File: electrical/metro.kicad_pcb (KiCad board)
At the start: 2 copper layers, 28 x 14 mm, 44 parts, among them Q1 AO3401A, Q2 AO3400A, SW1 SW_Push, SW2 SW_Push, SW3 SW_Push, U1 ATTINY1616-MN, U2 MCP73831-2-OT, U3 XC6206PxxxMR, Y1 32.678

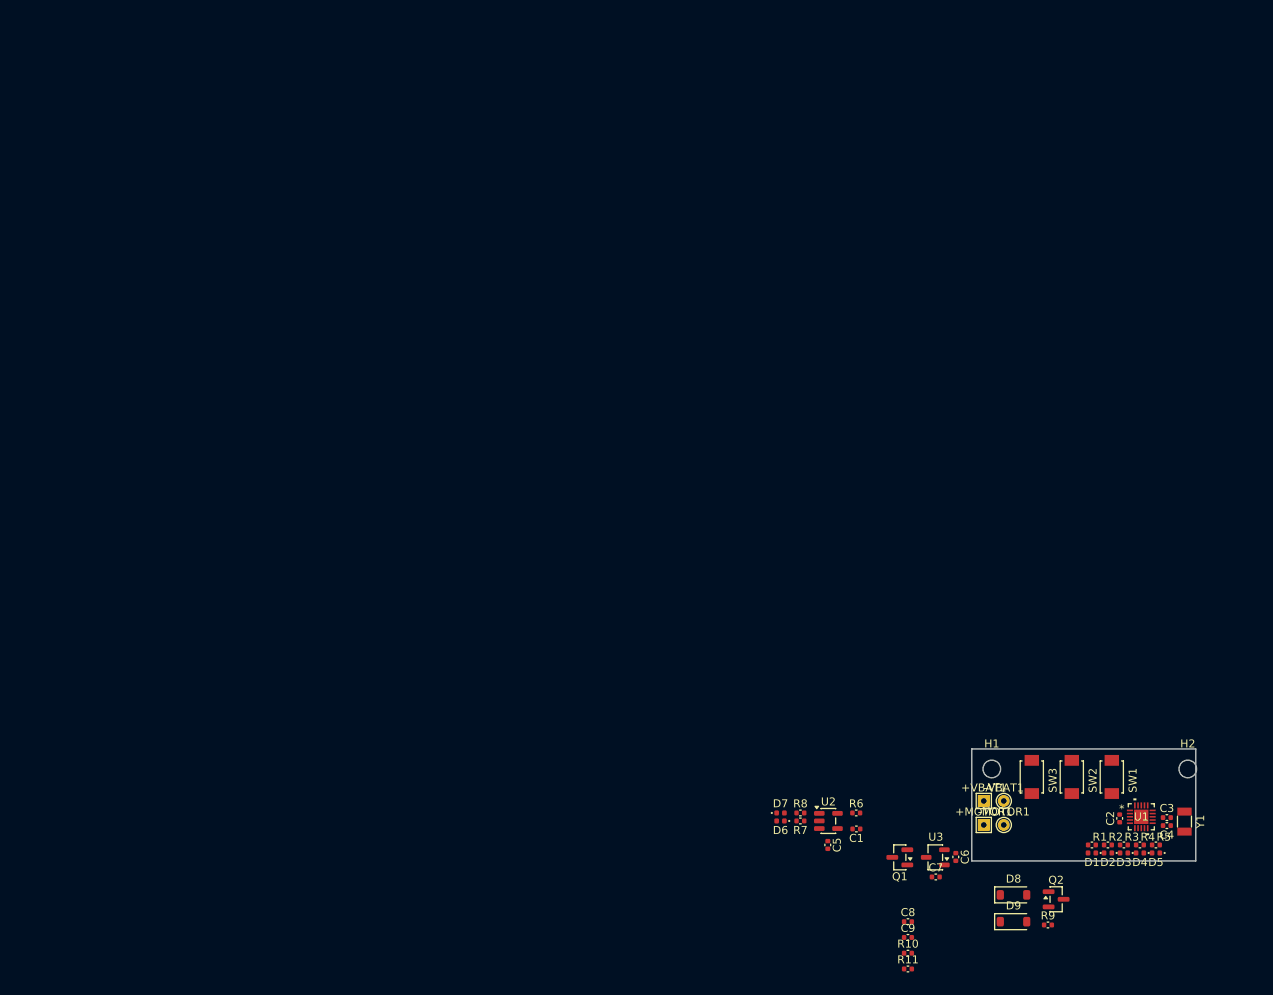
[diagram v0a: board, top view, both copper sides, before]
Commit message: Basic vibration with breakout board
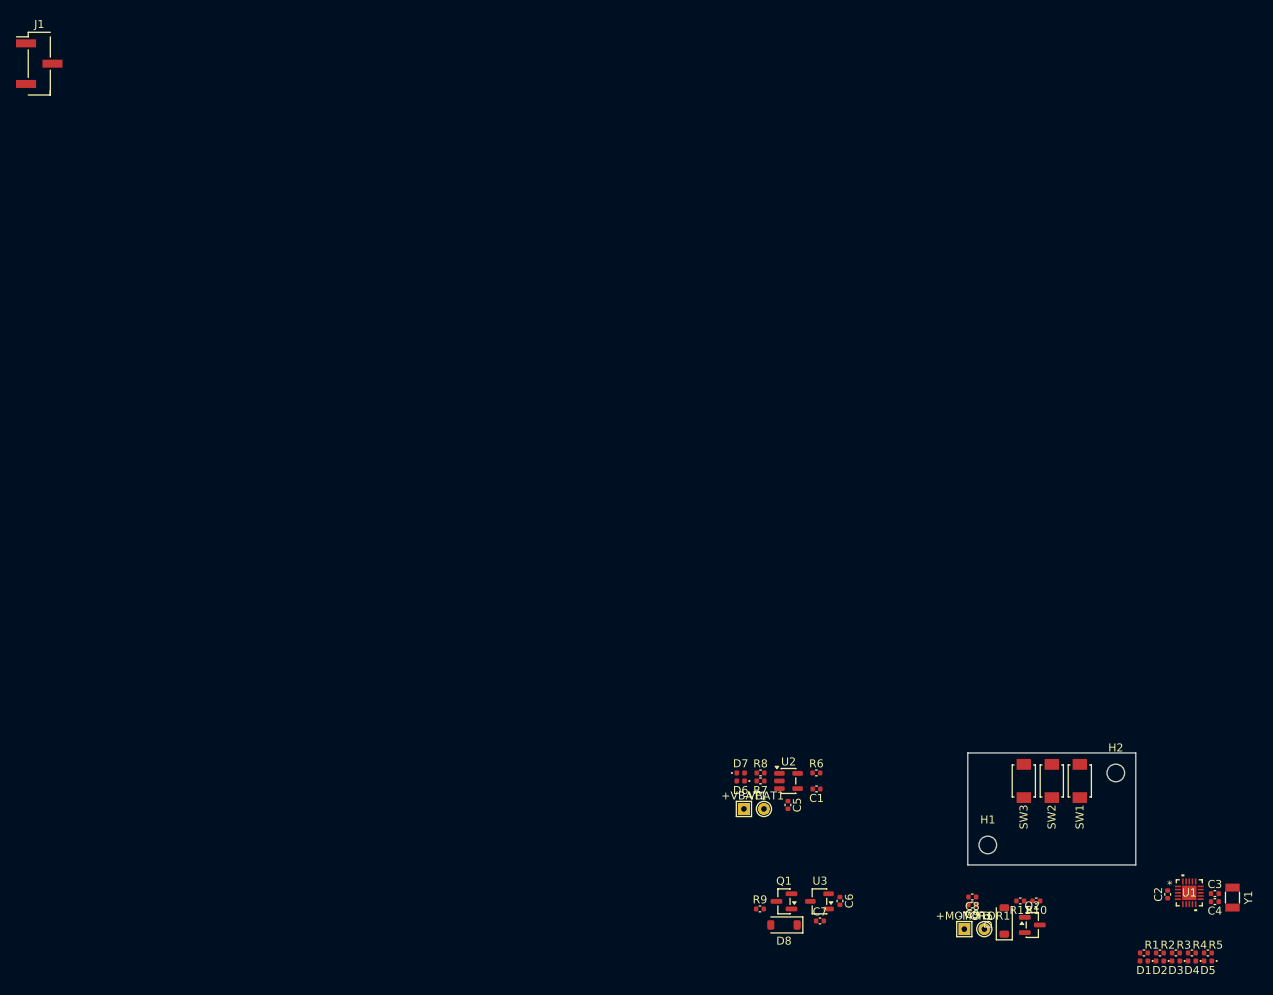
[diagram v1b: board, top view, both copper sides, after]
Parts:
- added J1: Conn_01x03_Pin, Connector_PinHeader_2.54mm:PinHeader_1x03_P2.54mm_Vertical_SMD_Pin1Left, F.Cu at (3.44, 4.33)
- moved R9 36.1 mm to (93.5, 110.0)
- moved +VBAT1 30.0 mm to (91.5, 97.5)
- moved -VBAT1 30.0 mm to (94.0, 97.5)
- moved D8 28.9 mm to (96.5, 112.0), turned to 180 degrees
- moved R10 17.3 mm to (128.1, 109.0), turned to 180 degrees
- moved R11 16.4 mm to (126.1, 109.0), turned to 180 degrees
- moved C6 15.5 mm to (103.5, 109.0)
- moved C7 15.5 mm to (101.0, 111.5)
- moved Q1 15.5 mm to (96.5, 109.0)
- moved U3 15.5 mm to (101.0, 109.0)
- moved D1 15.0 mm to (141.5, 116.5)
- moved D2 15.0 mm to (143.5, 116.5)
- moved D3 15.0 mm to (145.5, 116.5)
- moved D4 15.0 mm to (147.5, 116.5)
- moved D5 15.0 mm to (149.5, 116.5)
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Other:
- board size 28 x 14 mm -> 21 x 14 mm

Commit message: Circuit mostly complete with driver
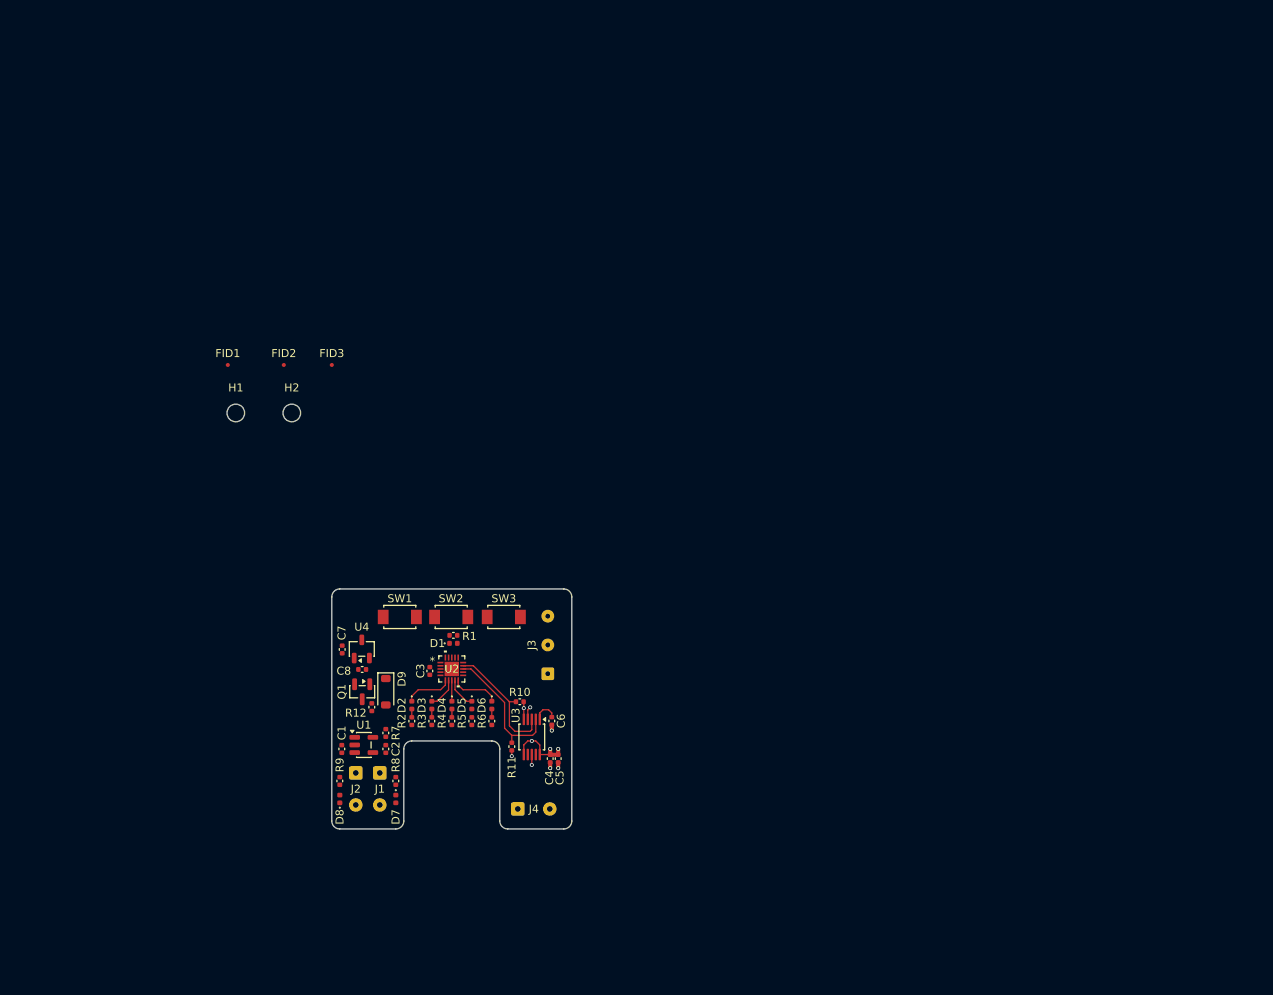
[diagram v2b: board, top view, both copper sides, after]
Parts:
- removed +MOTOR1, +VBAT1: ~, TestPoint:TestPoint_THTPad_1.5x1.5mm_Drill0.7mm
- removed -MOTOR1, -VBAT1: ~, TestPoint:TestPoint_THTPad_D1.5mm_Drill0.7mm
- removed the C3 at (150.4, 108.1)
- removed the C8 at (120.1, 108.5)
- removed C9: 10μF, Capacitor_SMD:C_0402_1005Metric
- removed the D9 at (124.1, 111.5)
- removed Q2: AO3400A, Package_TO_SOT_SMD:SOT-23
- removed Y1: 32.678, Crystal:Crystal_SMD_3215-2Pin_3.2x1.5mm
- added C5: 10μF, Capacitor_SMD:C_0402_1005Metric, F.Cu at (68.3, 91.2)
- added C6: 1μF, Capacitor_SMD:C_0402_1005Metric, F.Cu at (67.5, 86.5)
- added D1: Blue, LED_SMD:LED_0402_1005Metric, F.Cu at (55.2, 76.8)
- added FID1: Fiducial, Fiducial:Fiducial_0.5mm_Mask1mm, F.Cu at (27.0, 42.0)
- added FID2: Fiducial, Fiducial:Fiducial_0.5mm_Mask1mm, F.Cu at (34.0, 42.0)
- added FID3: Fiducial, Fiducial:Fiducial_0.5mm_Mask1mm, F.Cu at (40.0, 42.0)
- added J2: Conn_01x02, Connector_Wire:SolderWire-0.15sqmm_1x02_P4mm_D0.5mm_OD1.5mm, F.Cu at (43.0, 93.0)
- added J3: Conn_01x03, Connector_Wire:SolderWire-0.1sqmm_1x03_P3.6mm_D0.4mm_OD1mm, F.Cu at (67.0, 80.6)
- added J4: Conn_01x02, Connector_Wire:SolderWire-0.15sqmm_1x02_P4mm_D0.5mm_OD1.5mm, F.Cu at (63.2, 97.5)
- added R1: 2k2, Capacitor_SMD:C_0402_1005Metric, F.Cu at (55.2, 75.8)
- added U3: DRV2605LDGS, Package_SO:VSSOP-10_3x3mm_P0.5mm, F.Cu at (65.0, 88.5)
- C4: value 20pF -> 1μF
- J1: value Conn_01x03_Pin -> Conn_01x02; footprint Connector_PinHeader_2.54mm:PinHeader_1x03_P2.54mm_Vertical_SMD_Pin1Left -> Connector_Wire:SolderWire-0.15sqmm_1x02_P4mm_D0.5mm_OD1.5mm
- R10: value 100kR -> 4k7
- R11: value 100R -> 4k7
- R2: renamed from R1; value 680R -> 2k2
- R3: renamed from R2; value 680R -> 2k2
- R4: renamed from R3; value 680R -> 2k2
- R5: renamed from R4; value 680R -> 2k2
- R6: renamed from R5; value 680R -> 2k2
- R7: renamed from R6; value 10kR -> 33k
- R8: renamed from R7; value 680R -> 2k2
- R9: renamed from R8; value 680R -> 10k
- U1: renamed from U2; value MCP73831-2-OT -> MCP73831T-2ACI/OT
- U4: renamed from U3; value XC6206PxxxMR -> XC6206P332MR-G
- moved H2 112.4 mm to (35.0, 48.0)
- moved H1 108.4 mm to (28.0, 48.0)
- moved J1 98.4 mm to (46.0, 93.0), turned to -90 degrees
- moved D2 96.9 mm to (50.0, 84.5), turned to -90 degrees
- moved D3 96.5 mm to (52.5, 84.5), turned to -90 degrees
- moved C3 96.4 mm to (52.2, 80.2)
- moved U2 96.3 mm to (55.0, 80.0)
- moved R2 96.0 mm to (50.0, 86.5), turned to 90 degrees
- moved D4 96.0 mm to (55.0, 84.5), turned to -90 degrees
- moved D5 95.5 mm to (57.5, 84.5), turned to -90 degrees
- moved R3 95.5 mm to (52.5, 86.5), turned to 90 degrees
- moved D6 95.1 mm to (60.0, 84.5), turned to -90 degrees
- moved R4 95.0 mm to (55.0, 86.5), turned to 90 degrees
- moved R5 94.6 mm to (57.5, 86.5), turned to 90 degrees
- moved R6 94.1 mm to (60.0, 86.5), turned to 90 degrees
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- renumbered C5 to C1, C1 to C2, C2 to C3, C6 to C8, D1 to D2, D2 to D3, D3 to D4, D4 to D5, D5 to D6, D6 to D7, D7 to D8, D8 to D9, R9 to R12, SW3 to SW1, SW1 to SW3, U1 to U2
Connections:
- net +VBAT renamed +BATT
- net Net-(U2-STAT) renamed /LIPO STAT
- C2 pad 1: +5V -> +VBUS
- C4 pad 1: Net-(U1A-PB3/TOSC1) -> +3V3
- D7 pad 2: +5V -> +VBUS
- D9 pad 2: +5V -> +VBUS
- J1 pad 1: unconnected-(J1-Pin_1-Pad1) -> +VBUS
- J1 pad 2: unconnected-(J1-Pin_2-Pad2) -> GND
- Q1 pad 1: +5V -> +VBUS
- R10 pad 1: GND -> /SCL
- R10 pad 2: /MOTOR -> +3V3
- R11 pad 1: Net-(Q2-G) -> /SDA
- R11 pad 2: /MOTOR -> +3V3
- R12 pad 2: +5V -> +VBUS
- SW1 pad 1: GND -> /SW1
- SW1 pad 2: Net-(U1A-PC3) -> GND
- SW2 pad 1: GND -> /SW2
- SW2 pad 2: Net-(U1A-PC2) -> GND
- SW3 pad 1: GND -> /SW3
- SW3 pad 2: Net-(U1A-PC1) -> GND
- U1 pad 4: +5V -> +VBUS
- U2 pad 1: unconnected-(U1A-PA2-Pad1) -> /SW1
- U2 pad 11: Net-(U1A-PB3/TOSC1) -> unconnected-(U2A-PB3/TOSC1-Pad11)
- U2 pad 12: Net-(U1A-PB2/TOSC2) -> /SW2
- U2 pad 13: unconnected-(U1A-PB1-Pad13) -> /SDA
- U2 pad 14: unconnected-(U1A-PB0-Pad14) -> /SCL
- U2 pad 15: unconnected-(U1A-PC0-Pad15) -> /STATUS
- U2 pad 16: Net-(U1A-PC1) -> unconnected-(U2A-PC1-Pad16)
- U2 pad 17: Net-(U1A-PC2) -> /SW3
- U2 pad 18: Net-(U1A-PC3) -> unconnected-(U2A-PC3-Pad18)
- U2 pad 19: /UDPI -> /UPDI
- U2 pad 5: /LED1 -> unconnected-(U2A-PA4-Pad5)
- U2 pad 6: /MOTOR -> /LED1
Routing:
- net /SDA: track 0.00 -> 17.1 mm
- net /SCL: track 0.00 -> 15.7 mm
- net +3V3: track 0.00 -> 11.5 mm, vias 0 -> 5
- net /LED5: track 0.00 -> 5.99 mm
- net /LED1: track 0.00 -> 5.99 mm
- net GND: track 0.00 -> 5.08 mm, vias 0 -> 5
- net /LED2: track 0.00 -> 3.87 mm
- net /LED4: track 0.00 -> 3.87 mm
- net Net-(U3-REG): track 0.00 -> 3.15 mm
- net /LED3: track 0.00 -> 2.62 mm
- net Net-(D4-A): track 0.00 -> 1.04 mm
- net Net-(D6-A): track 0.00 -> 1.04 mm
- net Net-(D3-A): track 0.00 -> 1.04 mm
- net Net-(D2-A): track 0.00 -> 1.04 mm
- added copper zone on In2.Cu, net +3V3
- added copper zone on In1.Cu, net GND
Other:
- board size 21 x 14 mm -> 30 x 30 mm
- copper layers 2 -> 4

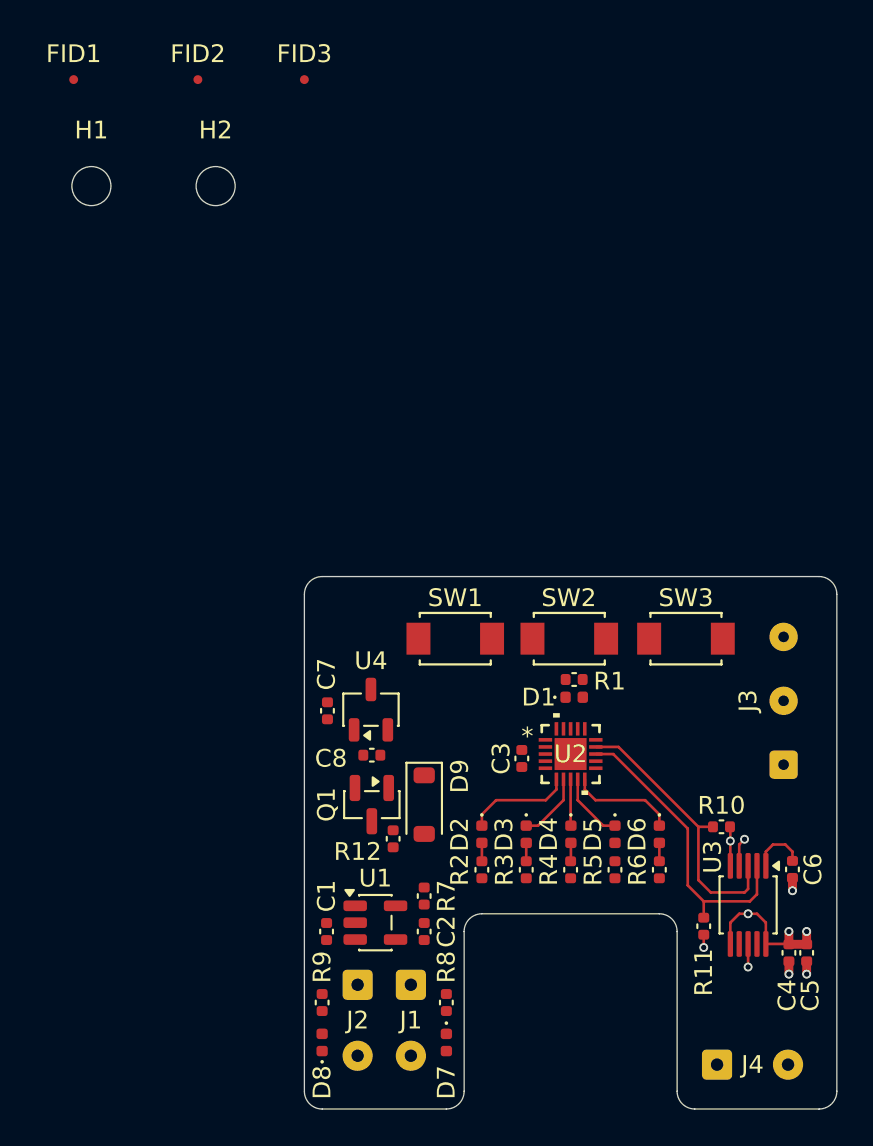
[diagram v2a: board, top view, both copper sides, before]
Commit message: new led setup
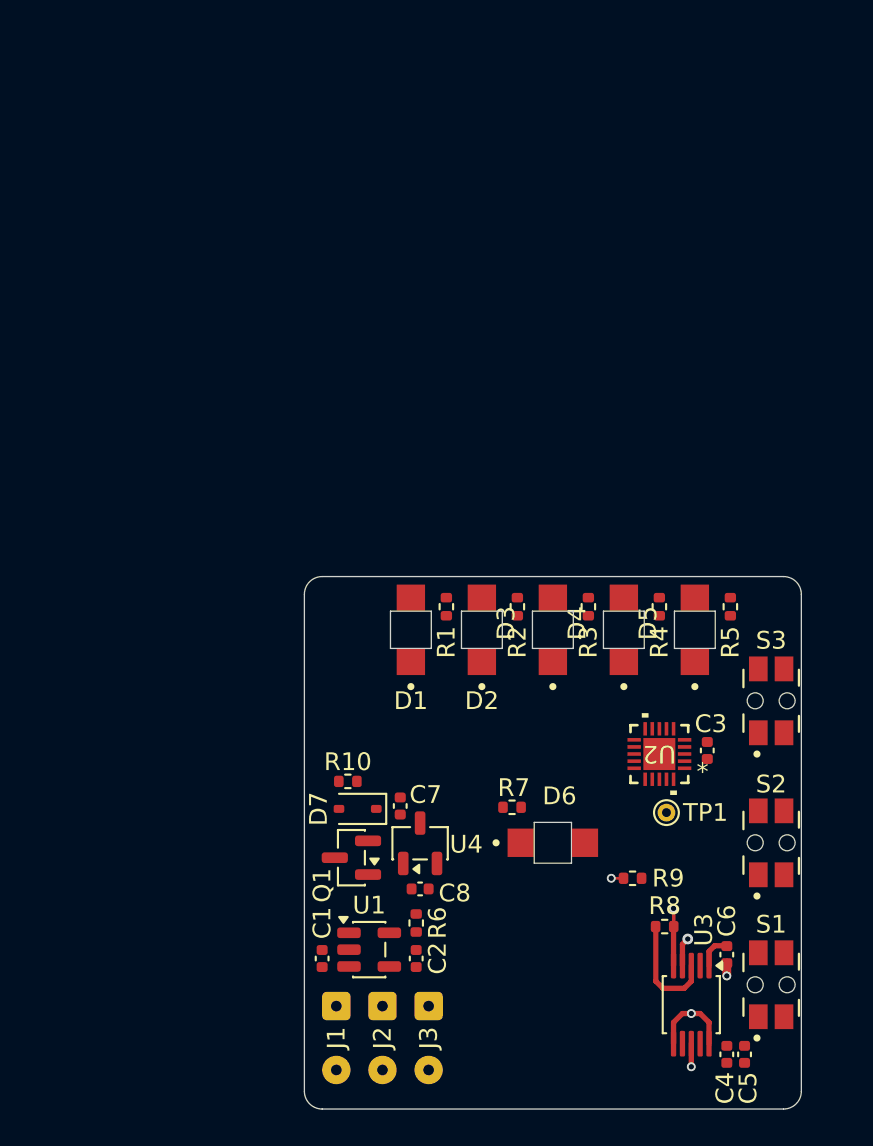
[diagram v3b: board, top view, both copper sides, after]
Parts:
- removed the D1 at (55.2, 76.8)
- removed D8: Green, LED_SMD:LED_0402_1005Metric
- removed FID1, FID2, FID3: Fiducial, Fiducial:Fiducial_0.5mm_Mask1mm
- removed H1, H2: M2, MountingHole:MountingHole_2.2mm_M2
- removed the J3 at (67.0, 80.6)
- removed the R1 at (55.2, 75.8)
- removed the R9 at (41.0, 94.0)
- removed SW1, SW2, SW3: SW_Push, TS-1088-AR02016:SW_TS-1088-AR02016
- added S1: EVQ-P7C01P, EVQ-P7C01P:SW_EVQ-P7C01P, F.Cu at (66.3, 93.0)
- added S2: EVQ-P7C01P, EVQ-P7C01P:SW_EVQ-P7C01P, F.Cu at (66.3, 85.0)
- added S3: EVQ-P7C01P, EVQ-P7C01P:SW_EVQ-P7C01P, F.Cu at (66.3, 77.0)
- added TP1: UPDI, TestPoint:TestPoint_THTPad_D1.0mm_Drill0.5mm, F.Cu at (60.4, 83.3)
- D1: renamed from D2; footprint LED_SMD:LED_0402_1005Metric -> LTST-C230KRKT:LED_LTST-C230KRKT
- D2: renamed from D3; footprint LED_SMD:LED_0402_1005Metric -> LTST-C230KRKT:LED_LTST-C230KRKT
- D3: renamed from D4; footprint LED_SMD:LED_0402_1005Metric -> LTST-C230KRKT:LED_LTST-C230KRKT
- D4: renamed from D5; footprint LED_SMD:LED_0402_1005Metric -> LTST-C230KRKT:LED_LTST-C230KRKT
- D5: renamed from D6; footprint LED_SMD:LED_0402_1005Metric -> LTST-C230KRKT:LED_LTST-C230KRKT
- D6: renamed from D7; footprint LED_SMD:LED_0402_1005Metric -> LTST-C230KRKT:LED_LTST-C230KRKT
- D7: renamed from D9; value D_Schottky -> 1N5819WS; footprint Diode_SMD:D_SOD-123 -> Diode_SMD:D_SOD-323
- J1: renamed from J2; footprint Connector_Wire:SolderWire-0.15sqmm_1x02_P4mm_D0.5mm_OD1.5mm -> Connector_Wire:SolderWire-0.1sqmm_1x02_P3.6mm_D0.4mm_OD1mm
- J2: renamed from J1; footprint Connector_Wire:SolderWire-0.15sqmm_1x02_P4mm_D0.5mm_OD1.5mm -> Connector_Wire:SolderWire-0.1sqmm_1x02_P3.6mm_D0.4mm_OD1mm
- J3: renamed from J4; footprint Connector_Wire:SolderWire-0.15sqmm_1x02_P4mm_D0.5mm_OD1.5mm -> Connector_Wire:SolderWire-0.1sqmm_1x02_P3.6mm_D0.4mm_OD1mm
- R1: renamed from R2; footprint Capacitor_SMD:C_0402_1005Metric -> Resistor_SMD:R_0402_1005Metric
- R10: renamed from R12; footprint Capacitor_SMD:C_0402_1005Metric -> Resistor_SMD:R_0402_1005Metric
- R2: renamed from R3; footprint Capacitor_SMD:C_0402_1005Metric -> Resistor_SMD:R_0402_1005Metric
- R3: renamed from R4; footprint Capacitor_SMD:C_0402_1005Metric -> Resistor_SMD:R_0402_1005Metric
- R4: renamed from R5; footprint Capacitor_SMD:C_0402_1005Metric -> Resistor_SMD:R_0402_1005Metric
- R5: renamed from R6; footprint Capacitor_SMD:C_0402_1005Metric -> Resistor_SMD:R_0402_1005Metric
- R6: renamed from R7; footprint Capacitor_SMD:C_0402_1005Metric -> Resistor_SMD:R_0402_1005Metric
- R7: renamed from R8; footprint Capacitor_SMD:C_0402_1005Metric -> Resistor_SMD:R_0402_1005Metric
- R8: renamed from R10; footprint Capacitor_SMD:C_0402_1005Metric -> Resistor_SMD:R_0402_1005Metric
- R9: renamed from R11; footprint Capacitor_SMD:C_0402_1005Metric -> Resistor_SMD:R_0402_1005Metric
- moved J3 16.6 mm to (47.0, 94.2), turned to -90 degrees
- moved R5 15.4 mm to (64.0, 71.7)
- moved R4 15.0 mm to (60.0, 71.7)
- moved R1 15.0 mm to (48.0, 71.7)
- moved R3 14.9 mm to (56.0, 71.7)
- moved R2 14.8 mm to (52.0, 71.7)
- moved D6 12.8 mm to (54.0, 85.0), turned to 0 degrees
- moved D1 12.2 mm to (46.0, 73.0), turned to 90 degrees
- moved D2 11.8 mm to (50.0, 73.0), turned to 90 degrees
- moved D5 11.7 mm to (62.0, 73.0), turned to 90 degrees
- moved R7 11.6 mm to (51.7, 83.0), turned to 0 degrees
- moved D3 11.6 mm to (54.0, 73.0), turned to 90 degrees
- moved D4 11.5 mm to (58.0, 73.0), turned to 90 degrees
- moved C3 10.5 mm to (62.7, 79.8), turned to -90 degrees
- moved U4 8.02 mm to (46.5, 85.0)
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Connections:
- net Net-(D9-K) renamed /REG IN
- R1 pad 2: Net-(D2-A) -> Net-(D1-PadA)
- R2 pad 2: Net-(D3-A) -> Net-(D2-PadA)
- R3 pad 2: Net-(D4-A) -> Net-(D3-PadA)
- R4 pad 2: Net-(D5-A) -> Net-(D4-PadA)
- R5 pad 2: Net-(D6-A) -> Net-(D5-PadA)
- R7 pad 2: Net-(D7-K) -> Net-(D6-PadC)
- U2 pad 1: /SW1 -> /SW3
- U2 pad 10: /LED5 -> /LED1
- U2 pad 15: /STATUS -> unconnected-(U2A-PC0-Pad15)
- U2 pad 17: /SW3 -> /SW1
- U2 pad 6: /LED1 -> /LED5
- U2 pad 7: /LED2 -> /LED4
- U2 pad 9: /LED4 -> /LED2
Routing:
- net /SDA: track 17.1 -> 0.00 mm
- net /SCL: track 15.7 -> 6.27 mm
- net /LED5: track 5.99 -> 0.00 mm
- net /LED1: track 5.99 -> 0.00 mm
- net /LED2: track 3.87 -> 0.00 mm
- net /LED4: track 3.87 -> 0.00 mm
- net +3V3: track 11.5 -> 8.74 mm, vias 5 -> 3
- net /LED3: track 2.62 -> 0.00 mm
- net GND: track 5.08 -> 3.64 mm, vias 5 -> 3
- net Net-(U3-REG): track 3.15 -> 1.94 mm
- net Net-(D4-A): track 1.04 -> 0.00 mm
- net Net-(D6-A): track 1.04 -> 0.00 mm
- net Net-(D3-A): track 1.04 -> 0.00 mm
- net Net-(D2-A): track 1.04 -> 0.00 mm
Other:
- board size 30 x 30 mm -> 28 x 30 mm
